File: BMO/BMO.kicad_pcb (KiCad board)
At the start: 4 copper layers, 82 x 89.5 mm, 132 parts, among them J1 EXT, J10 USB_C_Receptacle_USB2.0_16P, J11 BAT, J12 Conn_01x06, J13 SERVO, J14 Conn_01x06, J2 Conn_ST_STDC14, J3 TOF1_VL53L0X, J4 TOF2_VL53L0X, J5 COULEUR_I2C, J6 NEOPIXEL, J7 LIDAR_X2, J8 OLED_I2C, J9 Conn_01x06, Q1 MMDT2907A-7-F, Q2 DMP1045U-7, Q3 DMN313DLT-7, SW1 USER, SW2 SW_Push, SW3 nQON, U1 STM32G474RBTx, U2 MPU-6050, U3 SN74AHCT1G125DBVR, U4 USBLC6-2SC6, U5 AP2112K-3.3, U6 BQ27220YZFR, U7 BQ25896RTW, U8 DRV8833PWPR, Y1 16MHz

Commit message: updated serigraphy
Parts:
- moved C31 3.00 mm to (133.0, 112.0)
- moved C26 1.00 mm to (131.0, 112.0)
- moved C30 0.80 mm to (134.5, 112.2), turned to 90 degrees
- moved C45 0.25 mm to (155.0, 71.8)
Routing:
- net /Power/REGN: track 16.3 -> 13.9 mm, vias 3 -> 2
- net AOUT2: track 54.6 -> 53.7 mm, vias 3 -> 1
- net BOUT1: track 61.3 -> 62.1 mm
- net +3.3V: track 93.0 -> 93.8 mm, vias 25 -> 24
- net AOUT1: track 62.0 -> 61.5 mm, vias 2 -> 1
- net +5V: track 72.6 -> 73.0 mm, vias 30 -> 21
- net GND: track 140.3 -> 140.5 mm, vias 219 -> 233
- net /STM32G474RBT3/I2C3_SCL_ToF_TCS_MPU: vias 4 -> 3
- added copper zone on F.Cu, net BOUT1
- added copper zone on F.Cu, net BOUT2
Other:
- board text removed: "R12"
- board text removed: "R20"

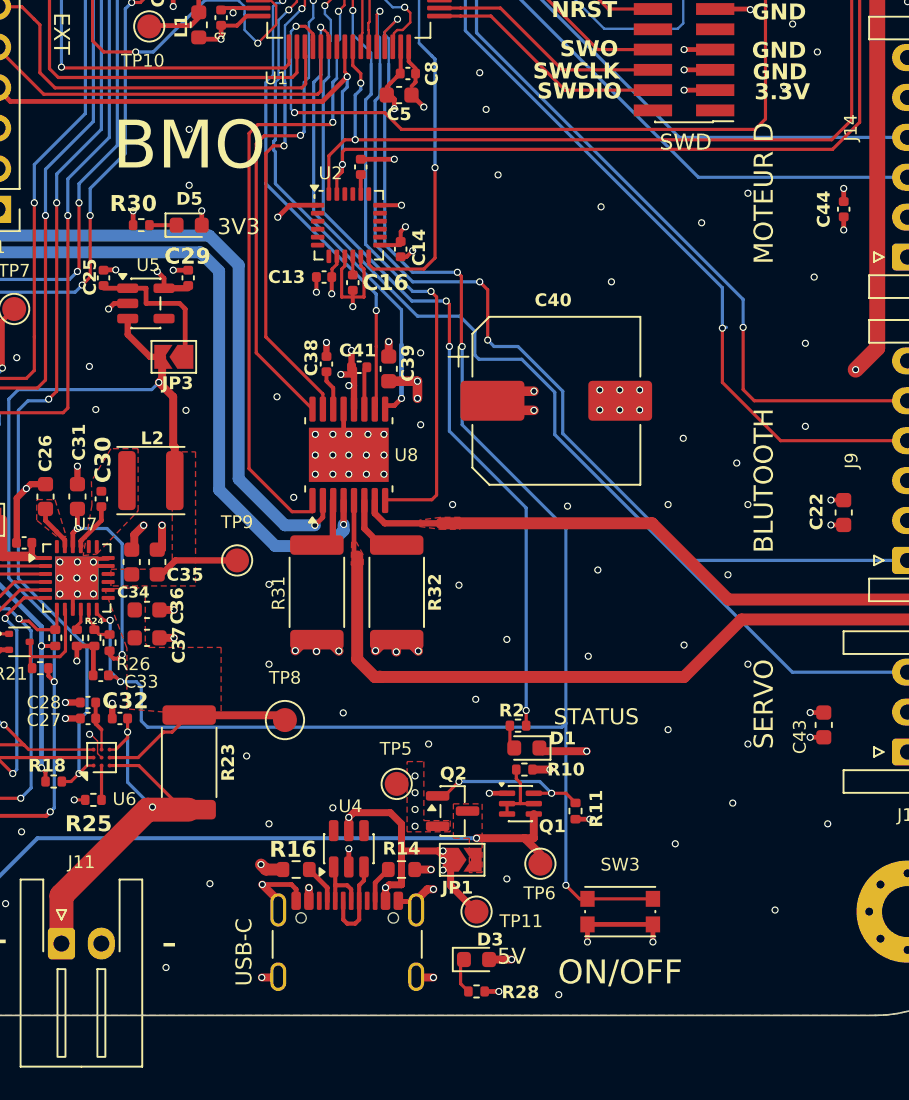
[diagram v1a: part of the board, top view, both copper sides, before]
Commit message: added on/off button, CSV completed and pcb updated
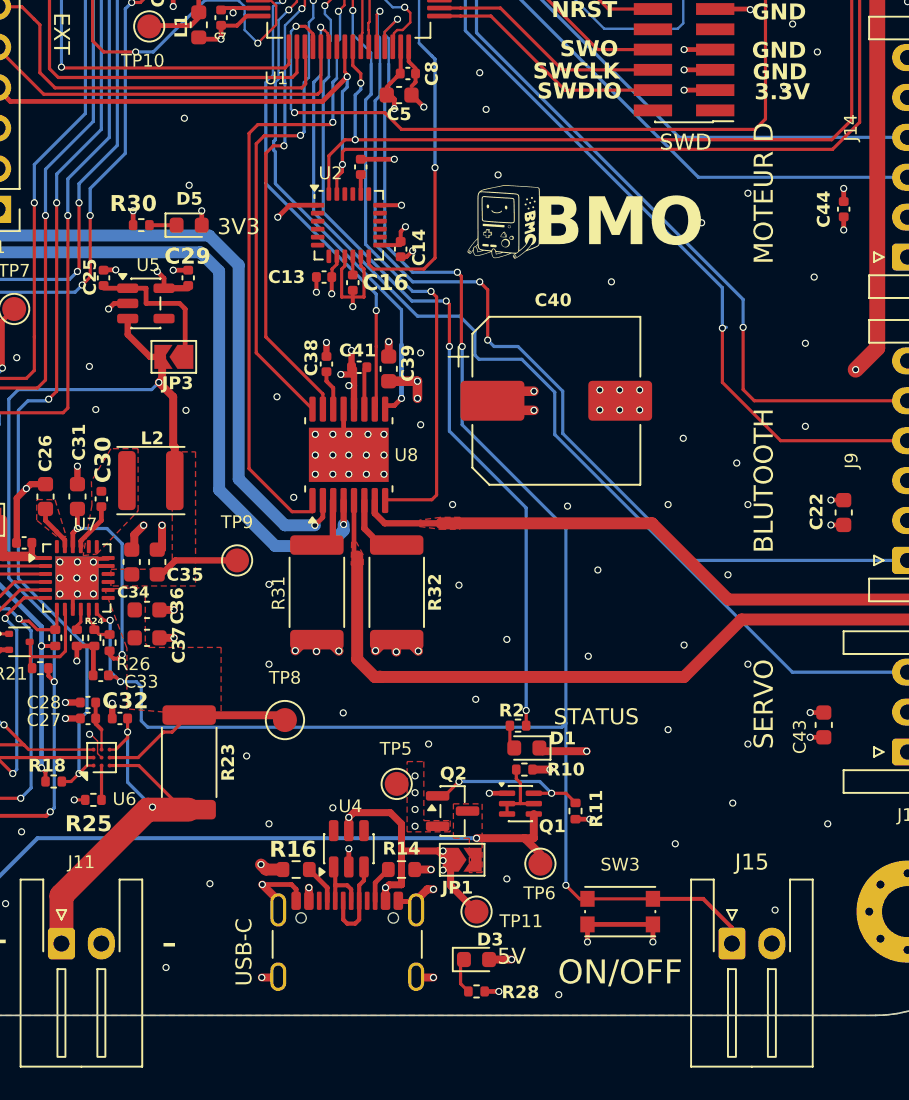
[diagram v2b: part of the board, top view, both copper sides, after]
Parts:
- added G***: LOGO, LOGO, F.Cu at (159.7, 94.8)
- added G***: LOGO, LOGO, B.Cu at (178.5, 128.4)
- added J15: ON/OFF, Connector_JST:JST_XH_S2B-XH-A-1_1x02_P2.50mm_Horizontal, F.Cu at (174.0, 140.0)
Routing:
- net /Power/PWR_Bouton: track 105.3 -> 112.0 mm
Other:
- board text removed: "ENSEA 3A ESE v1.0 2627"

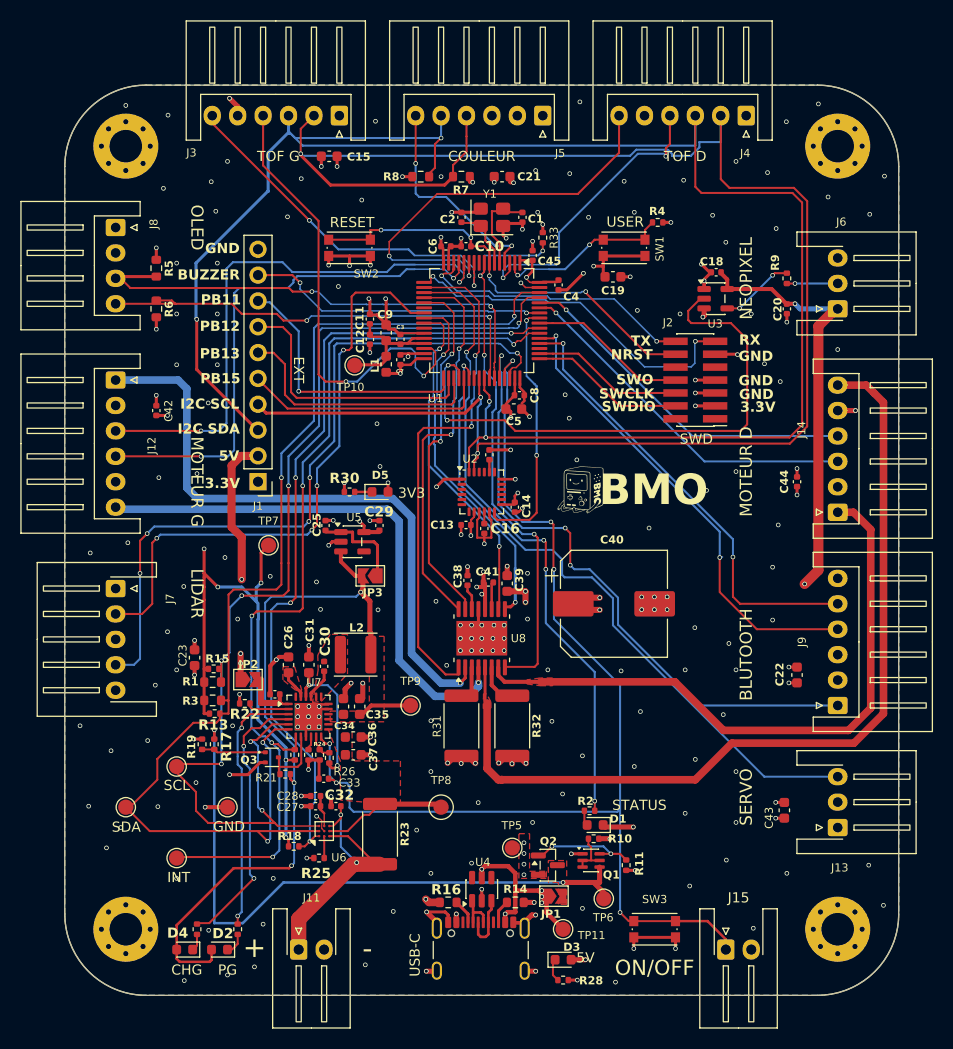
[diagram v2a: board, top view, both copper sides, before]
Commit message: Finalize PCB design and validate layout
- Apply layout and routing improvements
- Update components and footprint adjustments
- Run and pass design rule checks (DRC)
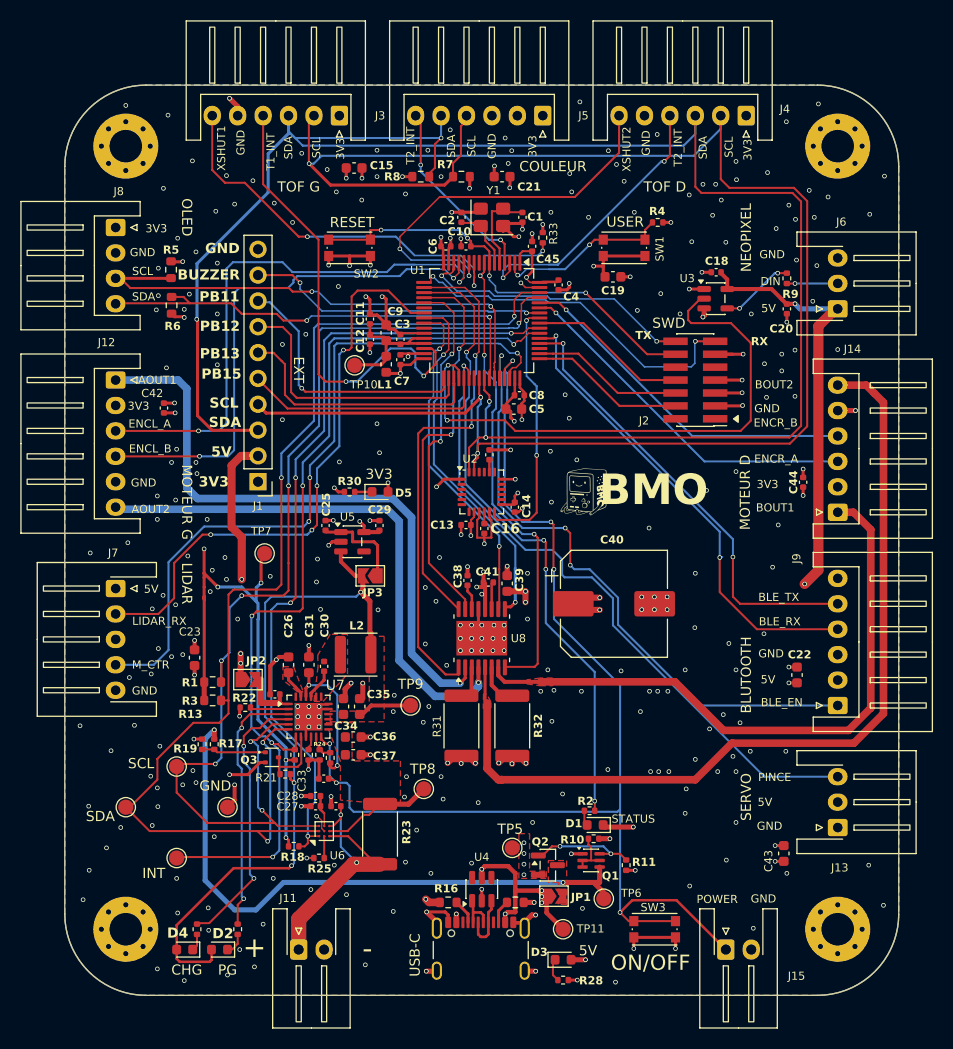
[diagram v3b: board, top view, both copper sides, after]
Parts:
- removed R13, R15: 1k5, Resistor_SMD:R_0402_1005Metric
- TP8: footprint TestPoint:TestPoint_Pad_D2.0mm -> TestPoint:TestPoint_Pad_D1.5mm
- moved C43 4.25 mm to (179.7, 130.6)
- moved C15 2.71 mm to (137.4, 63.1)
- moved TP8 2.48 mm to (144.3, 124.2)
- moved R6 1.54 mm to (119.5, 76.7)
- moved R5 1.46 mm to (119.5, 73.2)
- moved C45 0.90 mm to (154.9, 70.8)
- moved TP7 0.89 mm to (128.7, 101.0)
- moved C42 0.79 mm to (118.8, 86.8)
- moved C44 0.60 mm to (181.6, 94.0)
- moved R22 0.40 mm to (126.8, 116.2)
- moved G*** 0.36 mm to (160.0, 95.0)
- moved R26 0.09 mm to (135.1, 121.2)
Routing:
- net GND: track 140.5 -> 148.1 mm, vias 233 -> 331
- net /Power/PWR_Bouton: track 112.0 -> 118.2 mm
- net /STM32G474RBT3/I2C3_SCL_ToF_TCS_MPU: track 174.6 -> 171.6 mm
- net +3.3V: track 93.8 -> 96.6 mm
- net /STM32G474RBT3/XSHUT_TOF1: track 35.0 -> 37.7 mm
- net /STM32G474RBT3/XSHUT_TOF2: track 41.0 -> 38.7 mm
- net VBUS: track 63.0 -> 60.7 mm
- net /STM32G474RBT3/COLOR_INT: track 20.7 -> 18.8 mm
- net /STM32G474RBT3/TOF2_INT: track 28.2 -> 26.4 mm
- net /STM32G474RBT3/LIDAR_M_CTR_TIM16_CH1: track 70.7 -> 68.9 mm, vias 5 -> 3
- net /STM32G474RBT3/I2C2_SCL_OLED: track 48.5 -> 50.1 mm
- net /STM32G474RBT3/I2C3_SDA_ToF_TCS_MPU: track 182.9 -> 184.5 mm
- net /STM32G474RBT3/LIDARX2__USART1_RX: track 58.1 -> 56.8 mm
- net /Power/BAT: track 10.8 -> 9.61 mm
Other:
- board text added: "AOUT1"
- board text added: "AOUT2"
- board text added: "BLE_EN"
- board text added: "BLE_RX"
- board text added: "BLE_TX"
- board text added: "BOUT1"
- board text added: "BOUT2"
- board text added: "DIN"
- board text added: "ENCL_A"
- board text added: "ENCL_B"
- board text added: "ENCR_A"
- board text added: "ENCR_B"
- board text added: "LIDAR_RX"
- board text added: "M_CTR"
- board text added: "PINCE"
- board text added: "POWER"
- board text added: "T1_INT"
- board text added: "T2_INT"
- board text added: "XSHUT1"
- board text added: "XSHUT2"
- board text removed: "3.3V"
- board text removed: "C32"
- board text removed: "I2C SCL"
- board text removed: "I2C SDA"
- board text removed: "NRST"
- board text removed: "R26"
- board text removed: "SWCLK"
- board text removed: "SWDIO"
- board text removed: "SWO"
